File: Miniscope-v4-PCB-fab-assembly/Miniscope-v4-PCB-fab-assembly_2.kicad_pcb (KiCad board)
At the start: 6 copper layers, 30.2 x 18.8 mm, 64 parts, among them J1 Conn_01x01, J1 Conn_01x14, J1 Conn_01x20, J10 Conn_01x05, J2 Conn_01x01, J2 Conn_01x14, J3 Conn_01x01, J4 Conn_01x01, J5 Conn_01x01, J6 Conn_01x01, J7 Conn_01x01, J8 Conn_01x05, J9 Conn_01x01, Q1 MMBT3904LP-7B, U1 ATmega328-MU, U1 LMV321IDCKR, U1 MAX14574EWL+, U2 NOIP1SN0480A, U2 TPL0102-100RUCR, U3 LTC3218, U3 SiT_2.5mmx2mm

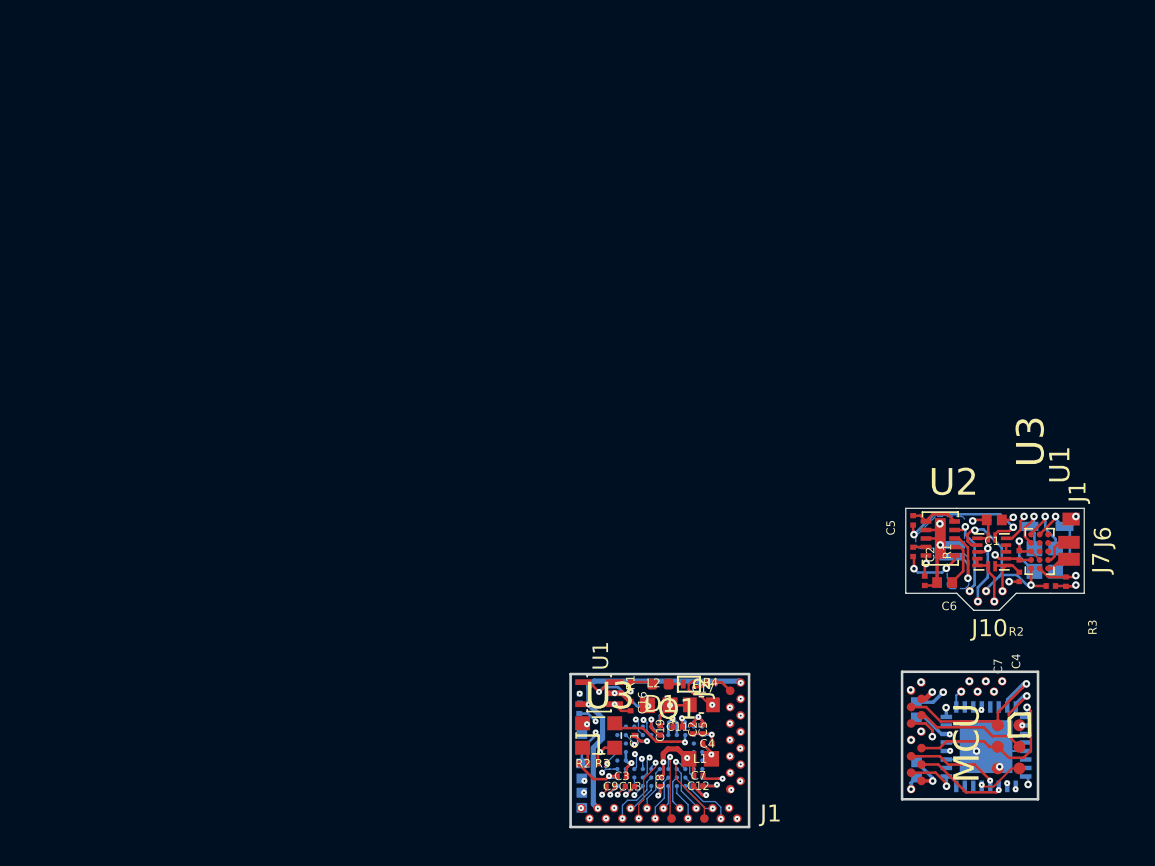
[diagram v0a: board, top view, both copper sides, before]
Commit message: Add final Miniscope v4 PCB layout that was submitted for fab on 05/03/2019
* Combined PYTHON480, MCU, LED-ETL-Driver, and Pow-Ser into a single PCB
* 2mm routing around PCBs
* 3mm tabs
* 2 4mm mounting holes
* 3 fiducials
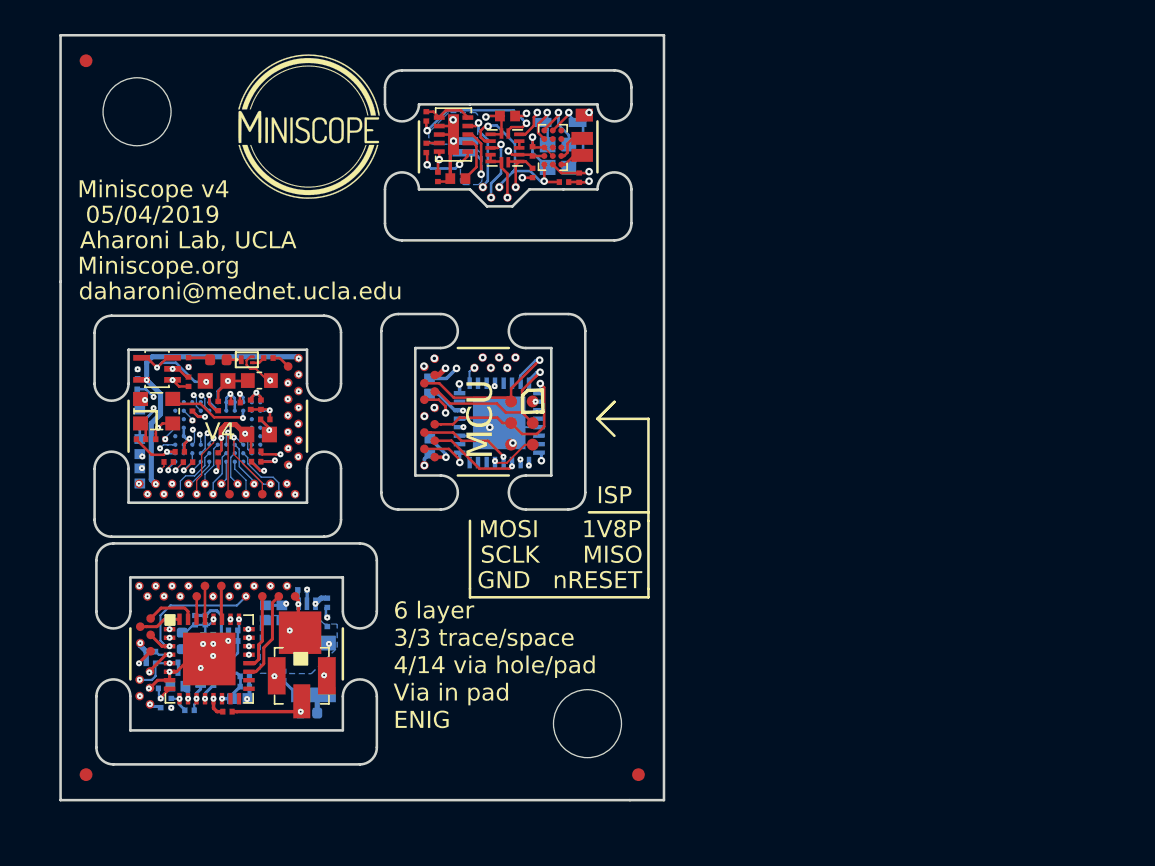
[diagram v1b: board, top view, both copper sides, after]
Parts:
- removed the C11 at (115.5, 126.6)
- removed the C19 at (114.5, 126.8)
- removed the R1 at (112.8, 124.2)
- removed the R4 at (117.5, 124.0)
- added C10: GRM033R61C473KE84D, .Capacitor:C_0201_0603Metric_L, B.Cu at (88.2, 123.9)
- added C11: GRM033R61A104ME15D, .Capacitor:C_0201_0603Metric_L, F.Cu at (89.5, 107.5)
- added C11: GRM033R61A105ME15D, .Capacitor:C_0201_0603Metric_L, B.Cu at (85.7, 125.2)
- added C18: GRM155R60J475ME47D, .Capacitor:C_0402_1005Metric_L, B.Cu at (87.5, 123.6)
- added C19: GRM033R61A104ME15D, .Capacitor:C_0201_0603Metric_L, F.Cu at (88.5, 107.7)
- added C19: GRM033R61A104ME15D, .Capacitor:C_0201_0603Metric_L, B.Cu at (87.6, 121.5)
- added C20: GRM033R71A103KA01D, .Capacitor:C_0201_0603Metric_L, B.Cu at (88.2, 121.4)
- added C21: GRM033R61A104ME15D, .Capacitor:C_0201_0603Metric_L, B.Cu at (89.4, 121.6)
- added C22: GRM033R71A103KA01D, .Capacitor:C_0201_0603Metric_L, B.Cu at (89.4, 120.9)
- added C23: GRM155R60J475ME47D, .Capacitor:C_0402_1005Metric_L, B.Cu at (86.1, 124.2)
- added C24: GRM033R61A104ME15D, .Capacitor:C_0201_0603Metric_L, B.Cu at (86.4, 122.8)
- added C25: GRM033R71A103KA01D, .Capacitor:C_0201_0603Metric_L, B.Cu at (86.4, 123.4)
- added C26: GRJ155R60J106ME11D, .Capacitor:C_0402_1005Metric_L, B.Cu at (89.8, 124.9)
- added C27: GRM033R61A104ME15D, .Capacitor:C_0201_0603Metric_L, B.Cu at (90.1, 123.6)
- added C28: GRM033R71A103KA01D, .Capacitor:C_0201_0603Metric_L, B.Cu at (90.1, 124.2)
- added C29: GRM033R61A104ME15D, .Capacitor:C_0201_0603Metric_L, B.Cu at (87.1, 120.3)
- added C30: GRM033R71A103KA01D, .Capacitor:C_0201_0603Metric_L, B.Cu at (87.7, 120.3)
- added C4: GRM155R60J106ME15D, .Capacitor:C_0402_1005Metric_L, B.Cu at (92.2, 119.9)
- added C5: GRM155R60J106ME15D, .Capacitor:C_0402_1005Metric_L, B.Cu at (91.3, 119.9)
- added C6: GRM033R61A105ME15D, .Capacitor:C_0201_0603Metric_L, B.Cu at (94.9, 119.3)
- added C7: GRM033R61A105ME15D, .Capacitor:C_0201_0603Metric_L, B.Cu at (94.9, 120.4)
- added C8: GRM033R61A105ME15D, .Capacitor:C_0201_0603Metric_L, B.Cu at (93.5, 118.6)
- added C9: GRM033R61A104ME15D, .Capacitor:C_0201_0603Metric_L, F.Cu at (89.0, 125.7)
- added G***: LOGO, .Logo:Miniscope_Logo2, F.Cu at (93.8, 91.3)
- added J16: Conn_01x20_Female, .Connector:B2B_Flex_20_Dual_Row_38milx24mil_Pad_20mil, F.Cu at (93.0, 118.9)
- added J_coax1: U_FL-R-SMT_10_, digikey-footprints:Coax_Conn_U.FL, F.Cu at (93.4, 123.6)
- added J_coax_gnd1: Conn_01x01, .Connector:Conn_1x1_100x100_Pad, F.Cu at (93.3, 121.1)
- added J_extra1: Conn_01x05, .Connector:B2B_Flex_05_Dual_Row_38milx24mil_Pad_20mil, F.Cu at (84.5, 120.2)
- added J_extra2: Conn_01x05, .Connector:B2B_Flex_05_Dual_Row_38milx24mil_Pad_20mil, F.Cu at (84.5, 123.3)
- added L1: ADL3225V-470MT-TL000, .Inductor:L_1210_3225Metric_L, B.Cu at (94.1, 123.2)
- added L2: BLM15HD102SN1D, Inductor_SMD:L_0402_1005Metric, B.Cu at (93.8, 125.8)
- added L4: BLM15HD102SN1D, Inductor_SMD:L_0402_1005Metric, B.Cu at (86.4, 121.5)
- added L5: BLM15HD102SN1D, Inductor_SMD:L_0402_1005Metric, B.Cu at (89.0, 123.0)
- added R1: 1.8K, .Resistor:R_0201_0603Metric_ERJ_L, F.Cu at (86.8, 105.2)
- added R1: MMBT3904LP-7B, .Resistor:R_0201_0603Metric_ERJ_L, B.Cu at (92.3, 123.6)
- added R2: ERJ-1GEF49R9C, .Resistor:R_0201_0603Metric_ERJ_L, B.Cu at (88.2, 122.7)
- added R3: ERJ-1GEF1002C, .Resistor:R_0201_0603Metric_ERJ_L, B.Cu at (85.1, 125.2)
- added R4: 1K, .Resistor:R_0201_0603Metric_ERJ_L, F.Cu at (91.5, 104.9)
- added R4: ERJ-1GEF1002C, .Resistor:R_0201_0603Metric_ERJ_L, B.Cu at (86.8, 125.6)
- added R5: ERJ-1GEF3321C, .Resistor:R_0201_0603Metric_ERJ_L, B.Cu at (84.5, 122.2)
- added R6: ERJ-1GEF3321C, .Resistor:R_0201_0603Metric_ERJ_L, B.Cu at (84.5, 122.9)
- added R7: ERJ-1GEF1003C, .Resistor:R_0201_0603Metric_ERJ_L, B.Cu at (84.7, 124.3)
- added REF**: Fiducial_0.75mm_Dia_1.5mm_Outer, Fiducial:Fiducial_0.75mm_Dia_1.5mm_Outer, F.Cu at (113.2, 129.4)
- added REF**: Fiducial_0.75mm_Dia_1.5mm_Outer, Fiducial:Fiducial_0.75mm_Dia_1.5mm_Outer, F.Cu at (80.7, 129.4)
- added REF**: Fiducial_0.75mm_Dia_1.5mm_Outer, Fiducial:Fiducial_0.75mm_Dia_1.5mm_Outer, F.Cu at (80.7, 87.4)
- added REF**: MountingHole_4mm, MountingHole:MountingHole_4mm, F.Cu at (83.7, 90.4)
- added REF**: MountingHole_4mm, MountingHole:MountingHole_4mm, F.Cu at (110.2, 126.4)
- added U1: DS90UB933-Q1, .Package_QFN:QFN_33_P50_500X500X80L40X24T310L, F.Cu at (88.0, 122.6)
- added U3: TLV7103318DSER, .Package_SON:SON_6_P50_150X150X80L50X25L, B.Cu at (93.7, 119.9)
- moved C1 37.2 mm to (105.5, 90.7)
- moved C2 37.2 mm to (101.4, 94.2)
- moved C3 37.2 mm to (109.1, 93.0)
- moved C4 37.2 mm to (107.0, 92.7)
- moved C7 37.2 mm to (107.0, 94.0)
- moved J1 37.2 mm to (110.0, 90.6)
- moved L1 37.2 mm to (107.9, 93.0)
- moved U1 37.2 mm to (108.2, 92.5)
- moved U2 37.2 mm to (105.4, 92.5)
- moved U3 37.2 mm to (102.3, 91.8)
- moved C5 37.2 mm to (100.7, 92.5)
- moved C6 37.2 mm to (102.6, 94.3)
- moved D1 37.2 mm to (108.6, 91.0)
- moved D2 37.2 mm to (103.0, 92.5)
- moved J10 37.2 mm to (104.1, 94.9)
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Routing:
- net +5V: track 17.5 -> 42.0 mm, vias 4 -> 7
- net GND: track 59.2 -> 80.9 mm, vias 33 -> 50
- net +3V3: track 21.9 -> 41.2 mm, vias 15 -> 18
- net VDDD: track 0.00 -> 9.59 mm, vias 0 -> 6
- net CLK_OUT: track 0.00 -> 9.04 mm, vias 0 -> 2
- net I2C_SDA: track 0.00 -> 8.43 mm, vias 0 -> 3
- net I2C_SCL: track 0.00 -> 6.45 mm, vias 0 -> 3
- net DIN0: track 0.00 -> 5.76 mm
- net DIN2: track 0.00 -> 5.10 mm, vias 0 -> 2
- net DOUT_P: track 0.00 -> 4.56 mm, vias 0 -> 1
- net DIN1: track 0.00 -> 4.46 mm
- net DIN3: track 0.00 -> 4.29 mm, vias 0 -> 2
- net DIN4: track 0.00 -> 3.78 mm, vias 0 -> 2
- net FV: track 0.00 -> 3.60 mm, vias 0 -> 2
- net Net-(L1-Pad1): track 0.00 -> 3.55 mm
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- added copper zone on B.Cu, net +5V
- added copper zone on In4.Cu, net VDDD
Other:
- board size 30.2 x 18.8 mm -> 35.5 x 45 mm
- net class Default: clearance 0.0889 -> 0.0762; trace_width 0.0889 -> 0.0762; via_dia 0.45 -> 0.3556; via_drill 0.2 -> 0.0762
- rule trace_clearance: 0.0889 -> 0.0762
- rule trace_min: 0.0889 -> 0.0762
- rule via_min_drill: 0.2 -> 0.0762
- rule via_min_size: 0.45 -> 0.3556
- board text added: "05/04/2019"
- board text added: "1V8P"
- board text added: "6 layer 3/3 trace/space 4/14 via hole/pad Via in pad ENIG"
- board text added: "Aharoni Lab, UCLA"
- board text added: "GND"
- board text added: "ISP"
- board text added: "MISO"
- board text added: "MOSI"
- board text added: "Miniscope v4"
- board text added: "Miniscope.org"
- board text added: "SCLK"
- board text added: "V4"
- board text added: "daharoni@mednet.ucla.edu"
- board text added: "nRESET"

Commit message: Add reference names to fiducials in PCB assembly
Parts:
- removed the REF** at (113.2, 129.4)
- removed the REF** at (80.7, 129.4)
- added REF_BL: Fiducial_0.75mm_Dia_1.5mm_Outer, Fiducial:Fiducial_0.75mm_Dia_1.5mm_Outer, F.Cu at (80.7, 129.4)
- added REF_BR: Fiducial_0.75mm_Dia_1.5mm_Outer, Fiducial:Fiducial_0.75mm_Dia_1.5mm_Outer, F.Cu at (113.2, 129.4)
- renumbered REF** to REF_TL
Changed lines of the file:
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@@
       (drillshape 0)
       (scaleselection 1)
-      (outputdirectory "Output/"))
+      (outputdirectory "Output/PnP/"))
   )
   (net 0 "")
@@
   (module .Logo:Miniscope_Logo2 (layer F.Cu)
     (at 93.83376 91.31452)
+    (attr smd)
     (fp_text reference G*** (at 0 0) (layer F.SilkS) hide
       (effects (font (size 1.524 1.524) (thickness 0.3)))
@@
     (descr "Circular Fiducial, 0.75mm bare copper top; 1.5mm keepout (Level B)")
     (tags marker)
-    (attr virtual)
-    (fp_text reference REF** (at 0 -2) (layer F.SilkS) hide
+    (attr smd)
+    (fp_text reference REF_BR (at 0 -2) (layer F.SilkS) hide
       (effects (font (size 1 1) (thickness 0.15)))
     )
@@
     (descr "Circular Fiducial, 0.75mm bare copper top; 1.5mm keepout (Level B)")
     (tags marker)
-    (attr virtual)
-    (fp_text reference REF** (at 0 -2) (layer F.SilkS) hide
+    (attr smd)
+    (fp_text reference REF_BL (at 0 -2) (layer F.SilkS) hide
       (effects (font (size 1 1) (thickness 0.15)))
     )
@@
     (descr "Circular Fiducial, 0.75mm bare copper top; 1.5mm keepout (Level B)")
     (tags marker)
-    (attr virtual)
-    (fp_text reference REF** (at 0 -2) (layer F.SilkS) hide
+    (attr smd)
+    (fp_text reference REF_TL (at 0 -2) (layer F.SilkS) hide
       (effects (font (size 1 1) (thickness 0.15)))
     )
@@
   (module .Connector:B2B_Flex_14_Dual_Row_38milx24mil_Pad_20mil (layer F.Cu)
     (at 93.22634 104.91798 270)
+    (attr smd)
     (fp_text reference J2 (at -1.5838 -0.033) (layer F.SilkS) hide
       (effects (font (size 1 1) (thickness 0.15)))
@@
   (module .Connector:B2B_Flex_20_Dual_Row_38milx24mil_Pad_20mil (layer F.Cu)
     (at 93.02634 112.91798 180)
+    (attr smd)
     (fp_text reference J1 (at -1.9856 0.2874 180) (layer F.SilkS) hide
       (effects (font (size 1 1) (thickness 0.15)))
@@
   (module .Connector:Conn_1x1_250x750_Pad (layer F.Cu)
     (at 110.04096 90.61492 90)
+    (attr smd)
     (fp_text reference J1 (at 1.6002 0.381 90) (layer F.SilkS) hide
       (effects (font (size 1 1) (thickness 0.15)))
@@
   (module .Connector:B2B_Flex_05_Dual_Row_38milx24mil_Pad_20mil (layer F.Cu)
     (at 104.076056 94.854434)
+    (attr smd)
     (fp_text reference J10 (at 1.164304 2.186686) (layer F.SilkS) hide
       (effects (font (size 1 1) (thickness 0.15)))
@@
   (module .Connector:Conn_1x1_250x750_Pad (layer F.Cu)
     (at 109.91396 92.98372 90)
+    (attr smd)
     (fp_text reference J7 (at -0.2 1.9 90) (layer F.SilkS) hide
       (effects (font (size 1 1) (thickness 0.15)))
@@
   (module .Connector:Conn_1x1_250x750_Pad (layer F.Cu)
     (at 109.91396 91.98372 90)
+    (attr smd)
     (fp_text reference J6 (at 0.3 2 90) (layer F.SilkS) hide
       (effects (font (size 1 1) (thickness 0.15)))
@@
   (module .Connector:Conn_1x1_700_Circular_Pad (layer F.Cu)
     (at 103.57752 105.48704 270)
+    (attr smd)
     (fp_text reference J9 (at -2.1684 0.7298 270) (layer F.SilkS) hide
       (effects (font (size 1 1) (thickness 0.15)))
@@
   (module .Connector:B2B_Flex_14_Dual_Row_38milx24mil_Pad_20mil (layer F.Cu)
     (at 101.24072 104.94564 270)
+    (attr smd)
     (fp_text reference J1 (at -1.627 0.393 270) (layer F.SilkS) hide
       (effects (font (size 1 1) (thickness 0.15)))
@@
   (module .Connector:B2B_Flex_05_Dual_Row_38milx24mil_Pad_20mil (layer F.Cu)
     (at 104.06012 104.87744)
+    (attr smd)
     (fp_text reference J8 (at 0.0376 -1.5588 90) (layer F.SilkS) hide
       (effects (font (size 1 1) (thickness 0.15)))
@@
   (module .Connector:Conn_1x1_700_Circular_Pad (layer F.Cu)
     (at 105.73232 110.00184 270)
+    (attr smd)
     (fp_text reference J7 (at 2.8168 0.1346 270) (layer F.SilkS) hide
       (effects (font (size 1 1) (thickness 0.15)))
@@
   (module .Connector:Conn_1x1_700_Circular_Pad (layer F.Cu)
     (at 107.00232 110.00184 270)
+    (attr smd)
     (fp_text reference J6 (at 1.0668 -2.0954 270) (layer F.SilkS) hide
       (effects (font (size 1 1) (thickness 0.15)))
@@
   (module .Connector:Conn_1x1_700_Circular_Pad (layer F.Cu)
     (at 105.73232 108.73184 270)
+    (attr smd)
     (fp_text reference J5 (at 4.0868 -1.413 270) (layer F.SilkS) hide
       (effects (font (size 1 1) (thickness 0.15)))
@@
   (module .Connector:Conn_1x1_700_Circular_Pad (layer F.Cu)
     (at 107.00232 108.73184 270)
+    (attr smd)
     (fp_text reference J4 (at 0.5868 -2.0954 270) (layer F.SilkS) hide
       (effects (font (size 1 1) (thickness 0.15)))
@@
   (module .Connector:Conn_1x1_700_Circular_Pad (layer F.Cu)
     (at 105.73232 107.46184 270)
+    (attr smd)
     (fp_text reference J3 (at -4.1432 -1.1154 270) (layer F.SilkS) hide
       (effects (font (size 1 1) (thickness 0.15)))
@@
   (module .Connector:Conn_1x1_700_Circular_Pad (layer F.Cu)
     (at 107.00232 107.46184 270)
+    (attr smd)
     (fp_text reference J2 (at 0.1068 -2.0954 270) (layer F.SilkS) hide
       (effects (font (size 1 1) (thickness 0.15)))
@@
   (module .Connector:Conn_1x1_100x100_Pad (layer F.Cu)
     (at 93.31596 121.06572 270)
+    (attr smd)
     (fp_text reference J_coax_gnd1 (at 0.2488 -5.5178 270) (layer F.SilkS) hide
       (effects (font (size 1 1) (thickness 0.15)))
@@
     (at 93.41756 123.60318)
     (descr https://media.digikey.com/pdf/Data%20Sheets/Hirose%20PDFs/UFL%20Series.pdf)
+    (attr smd)
     (fp_text reference J_coax1 (at 1.4162 -9.28866) (layer F.SilkS) hide
       (effects (font (size 1 1) (thickness 0.15)))
@@
   (module .Connector:B2B_Flex_05_Dual_Row_38milx24mil_Pad_20mil (layer F.Cu)
     (at 84.48946 123.349182 270)
+    (attr smd)
     (fp_text reference J_extra2 (at 1.965338 2.1557 270) (layer F.SilkS) hide
       (effects (font (size 1 1) (thickness 0.15)))
@@
   (module .Connector:B2B_Flex_05_Dual_Row_38milx24mil_Pad_20mil (layer F.Cu)
     (at 84.52502 120.230062 270)
+    (attr smd)
     (fp_text reference J_extra1 (at -1.915542 2.69126 270) (layer F.SilkS) hide
       (effects (font (size 1 1) (thickness 0.15)))
@@
   (module .Connector:B2B_Flex_20_Dual_Row_38milx24mil_Pad_20mil (layer F.Cu)
     (at 93.028936 118.92958 180)
+    (attr smd)
     (fp_text reference J16 (at 0.195176 2.61506 180) (layer F.SilkS) hide
       (effects (font (size 1 1) (thickness 0.15)))
